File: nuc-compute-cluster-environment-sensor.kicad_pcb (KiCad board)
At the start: 4 copper layers, 50 x 30 mm, 119 parts, among them J1 USB4105-GF-A, J2 SM04B-SRSS-TB-LF-SN, J3 SM04B-SRSS-TB-LF-SN, U1 FT4232H-56Q, U2 AP7370-33SA-7, U3 STM32G474CET6, U4 MB85RC1MTPNF-G, U5 SHT45, U6 BME280, Y1 ABM3B-12.000MHZ-B2-T, Y2 ECS-_327-12_5-34B-TR, Y3 ABM3B-8.000MHZ-10-1-U-T

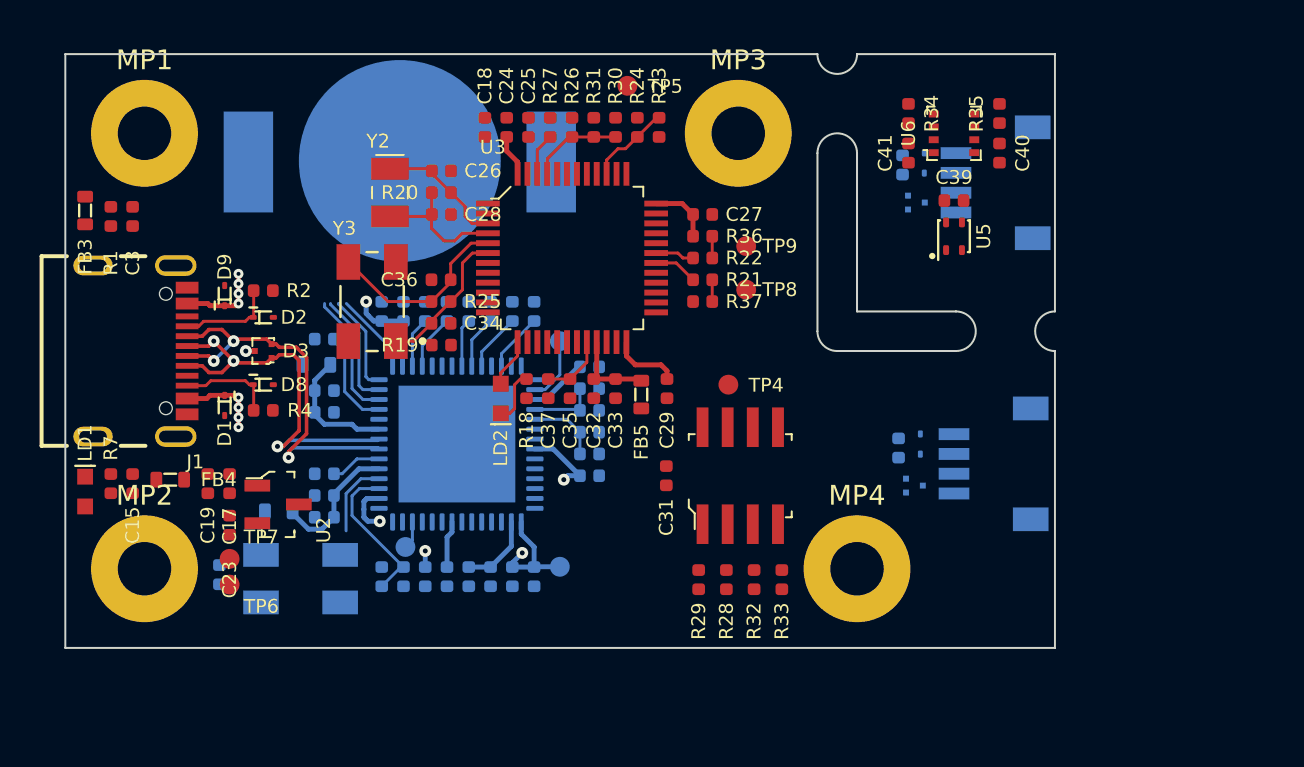
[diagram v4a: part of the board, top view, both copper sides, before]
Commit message: Initial routing, island part, USB and I2C buses finished
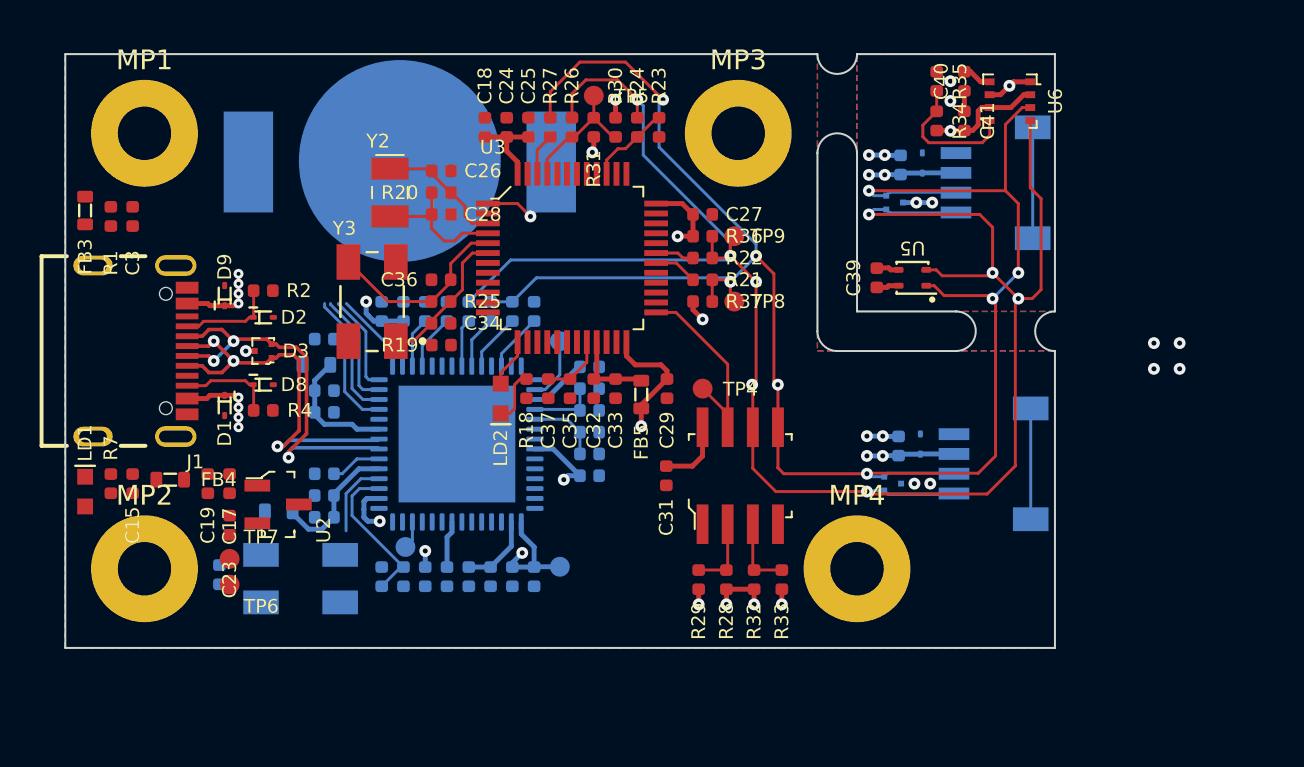
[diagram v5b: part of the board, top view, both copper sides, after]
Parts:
- moved C39 5.52 mm to (201.0, 121.3), turned to 90 degrees
- moved C40 4.04 mm to (205.4, 111.4), turned to 90 degrees
- moved R35 3.57 mm to (204.0, 111.4), turned to -90 degrees
- moved C41 3.26 mm to (205.4, 113.4), turned to -90 degrees
- moved U6 3.26 mm to (207.7, 112.4), turned to -90 degrees
- moved U5 2.97 mm to (202.8, 121.3), turned to 180 degrees
- moved TP5 1.77 mm to (186.7, 112.1)
- moved R34 1.47 mm to (204.0, 113.4)
- moved TP4 1.32 mm to (192.2, 126.9)
- moved D4 1.10 mm to (201.8, 131.7)
- moved D6 1.10 mm to (201.9, 117.5)
- moved TP8 0.85 mm to (193.8, 122.5)
- moved TP9 0.78 mm to (193.8, 119.2)
- moved C38 0.10 mm to (202.2, 115.6)
- moved C30 0.10 mm to (202.1, 129.8)
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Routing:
- net I2C_1_SCL: track 1.10 -> 101.0 mm, vias 0 -> 10
- net I2C_1_SDA: track 1.10 -> 97.6 mm, vias 0 -> 10
- net +3V3: track 23.6 -> 55.4 mm, vias 2 -> 13
- net GND: track 0.46 -> 12.0 mm, vias 1 -> 15
- net /FRAM_WP: track 0.00 -> 10.4 mm
- net Net-(R34-Pad1): track 0.00 -> 7.01 mm
- net Net-(BAT1-PadP): track 0.00 -> 5.60 mm, vias 0 -> 1
- net unconnected-(J3-PadS1): track 0.00 -> 5.60 mm
- net unconnected-(J2-PadS1): track 0.00 -> 5.60 mm
- net Net-(R28-Pad1): track 0.09 -> 3.74 mm
- net Net-(R32-Pad1): track 0.09 -> 3.74 mm
- net Net-(R26-Pad1): track 4.67 -> 6.59 mm
- added copper zone on In2.Cu, net +3V3
- added copper zone on B.Cu, net GND
- added copper zone on F.Cu, net GND
- added copper zone on In1.Cu, net GND

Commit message: Routing completed
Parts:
- turned C15 to 90 degrees
- turned C18 to -90 degrees
- turned C25 to 90 degrees
- turned C28 to 0 degrees
- turned C34 to 0 degrees
- turned LD1 to 90 degrees
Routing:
- net +3V3: track 55.4 -> 81.5 mm, vias 13 -> 26
- net JTDI: track 5.84 -> 30.4 mm, vias 0 -> 2
- net GNDREF: track 0.00 -> 21.7 mm
- net SWCLK-JTCK: track 6.46 -> 27.6 mm, vias 0 -> 2
- net /FTDI_USER_PB: track 0.00 -> 20.3 mm, vias 0 -> 4
- net SWDIO-JTMS: track 4.13 -> 24.2 mm, vias 0 -> 2
- net /FTDI_+1V8: track 12.2 -> 31.8 mm, vias 3 -> 4
- net LPUART_1_STM_TX: track 0.00 -> 19.5 mm, vias 0 -> 2
- net JTDO: track 5.00 -> 24.5 mm, vias 0 -> 2
- net Net-(BAT1-PadP): track 5.60 -> 24.7 mm
- net LPUART_1_STM_RX: track 0.00 -> 14.5 mm, vias 0 -> 3
- net Net-(C17-Pad1): track 0.00 -> 14.0 mm
- net Net-(C14-Pad2): track 3.86 -> 15.6 mm
- net NRST: track 0.00 -> 11.5 mm, vias 0 -> 1
- net JTRST: track 0.00 -> 11.4 mm, vias 0 -> 1
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- added copper zone on In2.Cu, net /VBUS

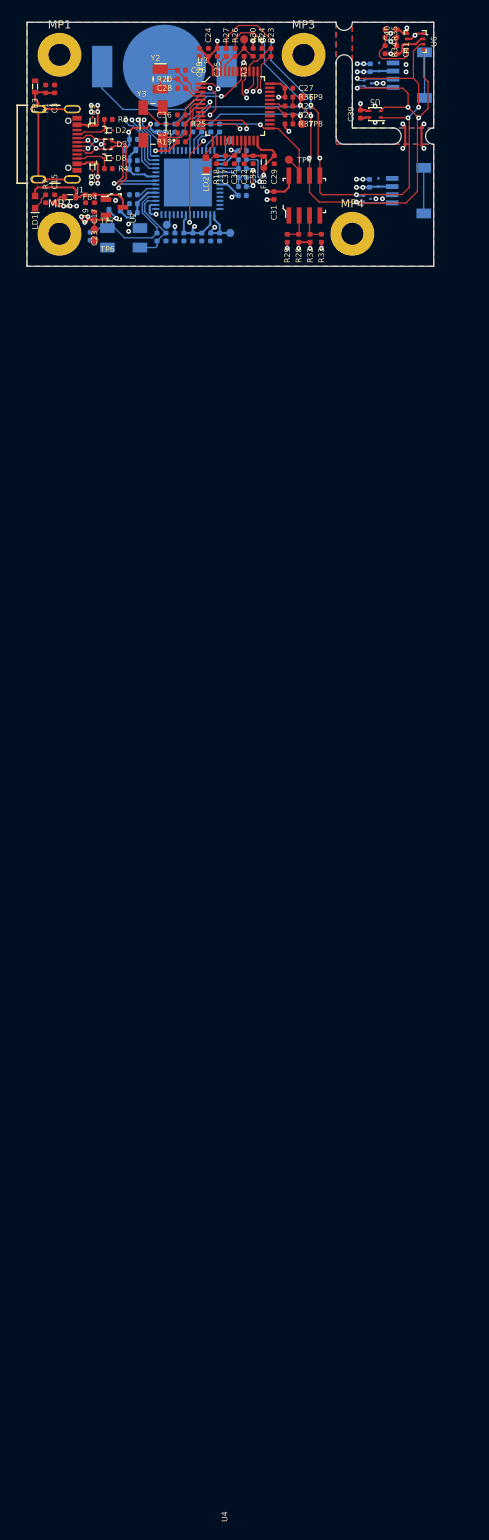
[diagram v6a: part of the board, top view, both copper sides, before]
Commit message: New component placement after review, all components moved to top layer except battery and connector
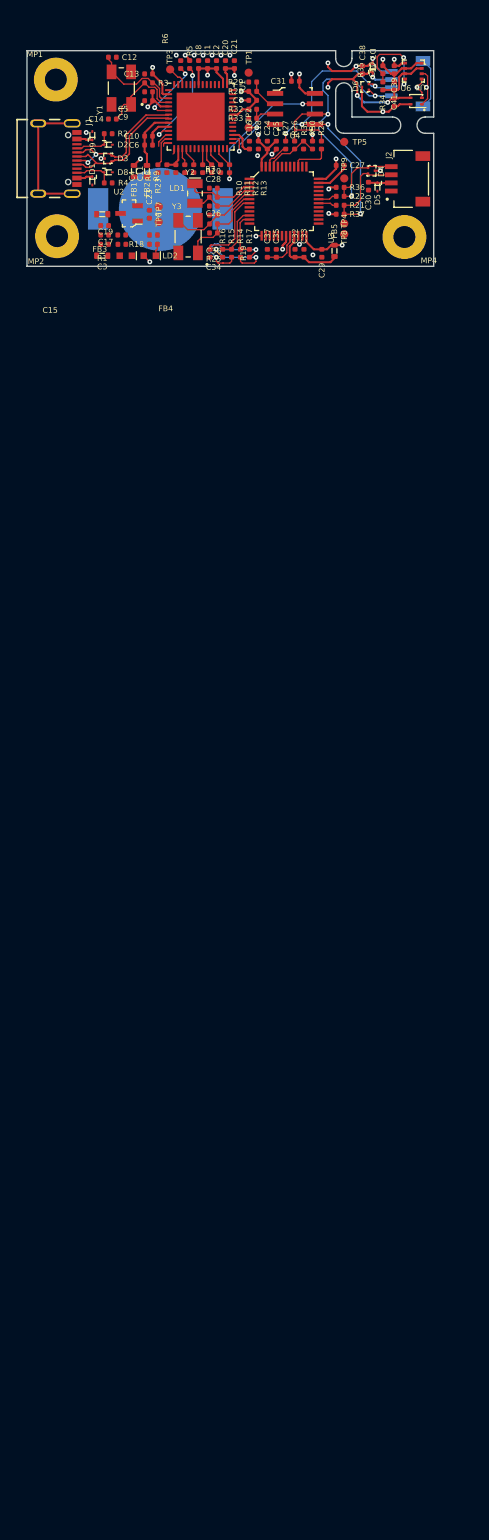
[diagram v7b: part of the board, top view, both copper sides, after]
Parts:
- removed MP3: PCB_Mount_Hole_2.7mm_M2.5_pad, antmicro-footprints:mounting-hole-2.7mm-M2.5-Pad
- C1, C10, C11, C12, C13, C14, C16, C2, C20, C21, C30, C38, C4, C5, C6, C7, C8, C9, D4, D5, D6, D7, FB1, FB2, J2, R10, R11, R12, R13, R14, R15, R16, R17, R3, R5, R6, R8, R9, TP1, TP2, TP3, U1, Y1: moved to F.Cu
- moved C12 23.1 mm to (170.5, 114.3), turned to 180 degrees
- moved C2 21.3 mm to (183.3, 115.2), turned to 90 degrees
- moved C20 21.3 mm to (184.4, 115.2), turned to 90 degrees
- moved C21 21.3 mm to (185.5, 115.2), turned to 90 degrees
- moved C1 21.3 mm to (182.2, 115.2), turned to 90 degrees
- moved C8 21.3 mm to (181.1, 115.2), turned to 90 degrees
- moved C13 20.3 mm to (174.9, 116.3), turned to 180 degrees
- moved R23 19.9 mm to (176.1, 128.0), turned to -90 degrees
- moved TP1 19.8 mm to (187.2, 116.2), turned to -90 degrees
- moved R29 19.7 mm to (187.8, 117.3), turned to 0 degrees
- moved TP3 19.1 mm to (177.6, 115.8), turned to 0 degrees
- moved R3 19.0 mm to (174.9, 117.5), turned to 0 degrees
- moved C3 19.0 mm to (169.6, 136.2), turned to 0 degrees
- moved R28 18.9 mm to (187.8, 118.5), turned to 180 degrees
- moved Y1 18.4 mm to (171.6, 118.1), turned to 180 degrees
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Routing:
- net I2C_1_SCL: track 100.2 -> 56.3 mm, vias 8 -> 4
- net I2C_1_SDA: track 97.6 -> 61.1 mm, vias 8 -> 6
- net GND: track 16.1 -> 51.1 mm, vias 29 -> 21
- net JTDI: track 30.4 -> 3.96 mm, vias 2 -> 0
- net SWCLK-JTCK: track 27.6 -> 2.11 mm, vias 2 -> 0
- net Net-(BAT1-PadP): track 24.7 -> 0.00 mm, vias 1 -> 0
- net JTDO: track 24.5 -> 0.95 mm, vias 2 -> 0
- net SWDIO-JTMS: track 24.2 -> 0.72 mm, vias 2 -> 0
- net /FTDI_USER_PB: track 20.3 -> 0.00 mm, vias 4 -> 0
- net /FTDI_+1V8: track 31.8 -> 11.9 mm, vias 4 -> 2
- net /LD2: track 2.45 -> 17.5 mm, vias 0 -> 2
- net Net-(C17-Pad1): track 14.0 -> 0.00 mm
- net LPUART_1_STM_TX: track 19.5 -> 6.62 mm, vias 2 -> 0
- net JTRST: track 11.4 -> 0.00 mm, vias 1 -> 0
- net /VBUS: track 14.5 -> 3.90 mm, vias 7 -> 0
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- removed copper zone on In2.Cu, net +3V3
- removed copper zone on In2.Cu, net /VBUS
- removed copper zone on B.Cu, net GND
- removed copper zone on F.Cu, net GND
- removed copper zone on In1.Cu, net GND
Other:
- board size 50 x 30 mm -> 50 x 26.5 mm

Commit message: Routing finished
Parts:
- moved TP2 8.25 mm to (187.2, 114.7)
- moved C19 0.95 mm to (172.6, 136.2)
- moved C17 0.94 mm to (172.6, 137.3)
- moved D1 0.05 mm to (168.0, 129.6)
- moved R4 0.05 mm to (170.0, 129.8), turned to 0 degrees
- turned C16 to -90 degrees
- turned D2 to 180 degrees
- turned D8 to 180 degrees
- turned R18 to 180 degrees
- turned R19 to 90 degrees
- turned R2 to 0 degrees
- turned R23 to 90 degrees
- turned R8 to 90 degrees
- turned R9 to 90 degrees
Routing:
- net SWCLK-JTCK: track 2.11 -> 26.1 mm, vias 0 -> 2
- net Net-(R23-Pad2): track 4.84 -> 28.7 mm, vias 0 -> 2
- net I2C_1_SDA: track 61.1 -> 84.7 mm, vias 6 -> 7
- net SWDIO-JTMS: track 0.72 -> 22.3 mm, vias 0 -> 2
- net I2C_1_SCL: track 56.3 -> 77.8 mm, vias 4 -> 5
- net /FRAM_WP: track 17.3 -> 38.4 mm
- net /FTDI_+1V8: track 11.9 -> 32.5 mm, vias 2 -> 3
- net JTDO: track 0.95 -> 20.2 mm, vias 0 -> 2
- net JTRST: track 0.00 -> 18.6 mm, vias 0 -> 2
- net Net-(R14-Pad1): track 9.74 -> 27.9 mm, vias 2 -> 3
- net /FTDI_USER_PB: track 0.00 -> 17.5 mm, vias 0 -> 2
- net Net-(R15-Pad1): track 12.0 -> 29.3 mm, vias 2 -> 3
- net GND: track 51.1 -> 66.8 mm, vias 21 -> 40
- net NRST: track 9.37 -> 22.5 mm, vias 0 -> 2
- net /VBUS: track 3.90 -> 11.5 mm, vias 0 -> 6
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- added copper zone on F.Cu, net +3V3
- added copper zone on In2.Cu, net +3V3
- added copper zone on In2.Cu, net /VBUS
- added copper zone on B.Cu, net GND
- added copper zone on F.Cu, net GND
- added copper zone on In1.Cu, net GND
